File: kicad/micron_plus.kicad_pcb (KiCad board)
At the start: 2 copper layers, 163.8 x 123.2 mm, 87 parts, among them J1 Conn_02x17_Odd_Even, J2 Cliff DC10A, Q1 2N2905A, Q2 2N2905A, Q3 2N3904, Q4 2N3904, U1 MC68A21, U10 74LS00, U11 7406, U12 HM6264LP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

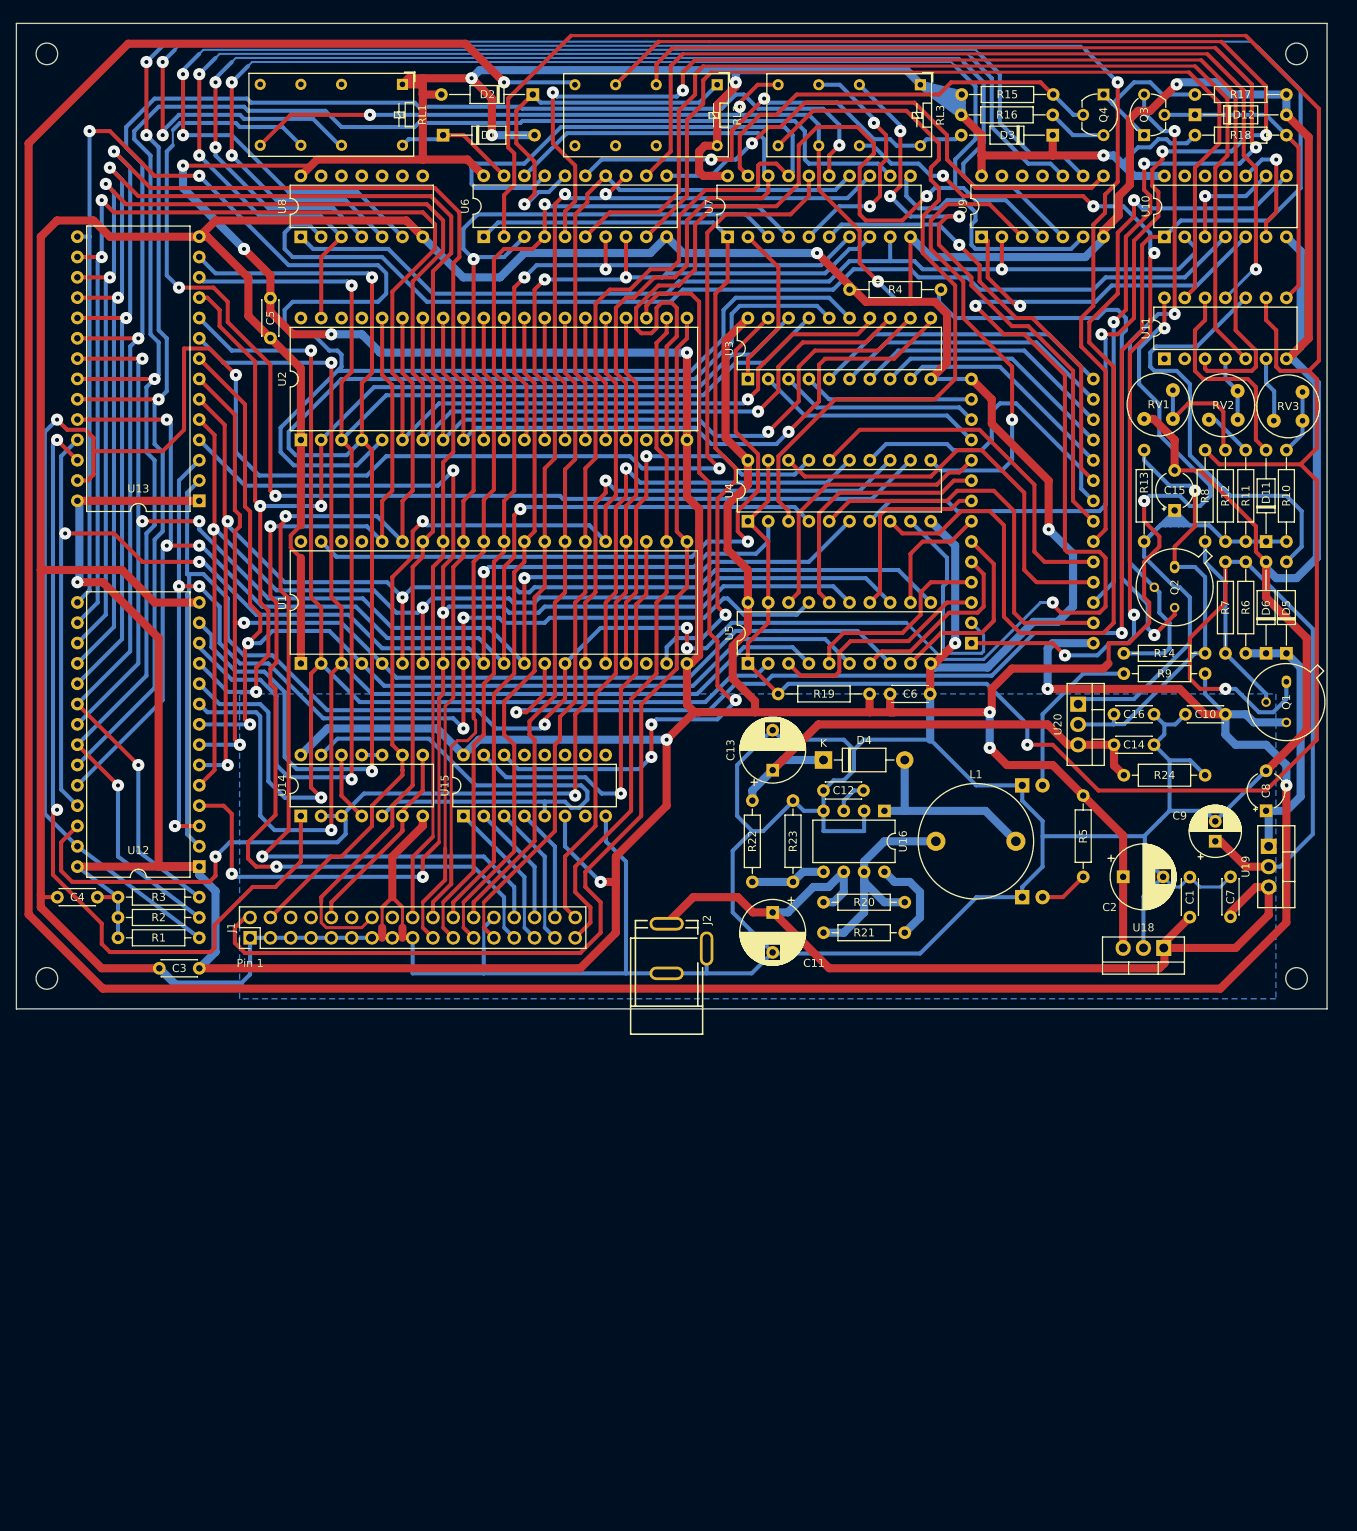
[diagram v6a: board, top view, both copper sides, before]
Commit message: KiCAD: Add heatsinks
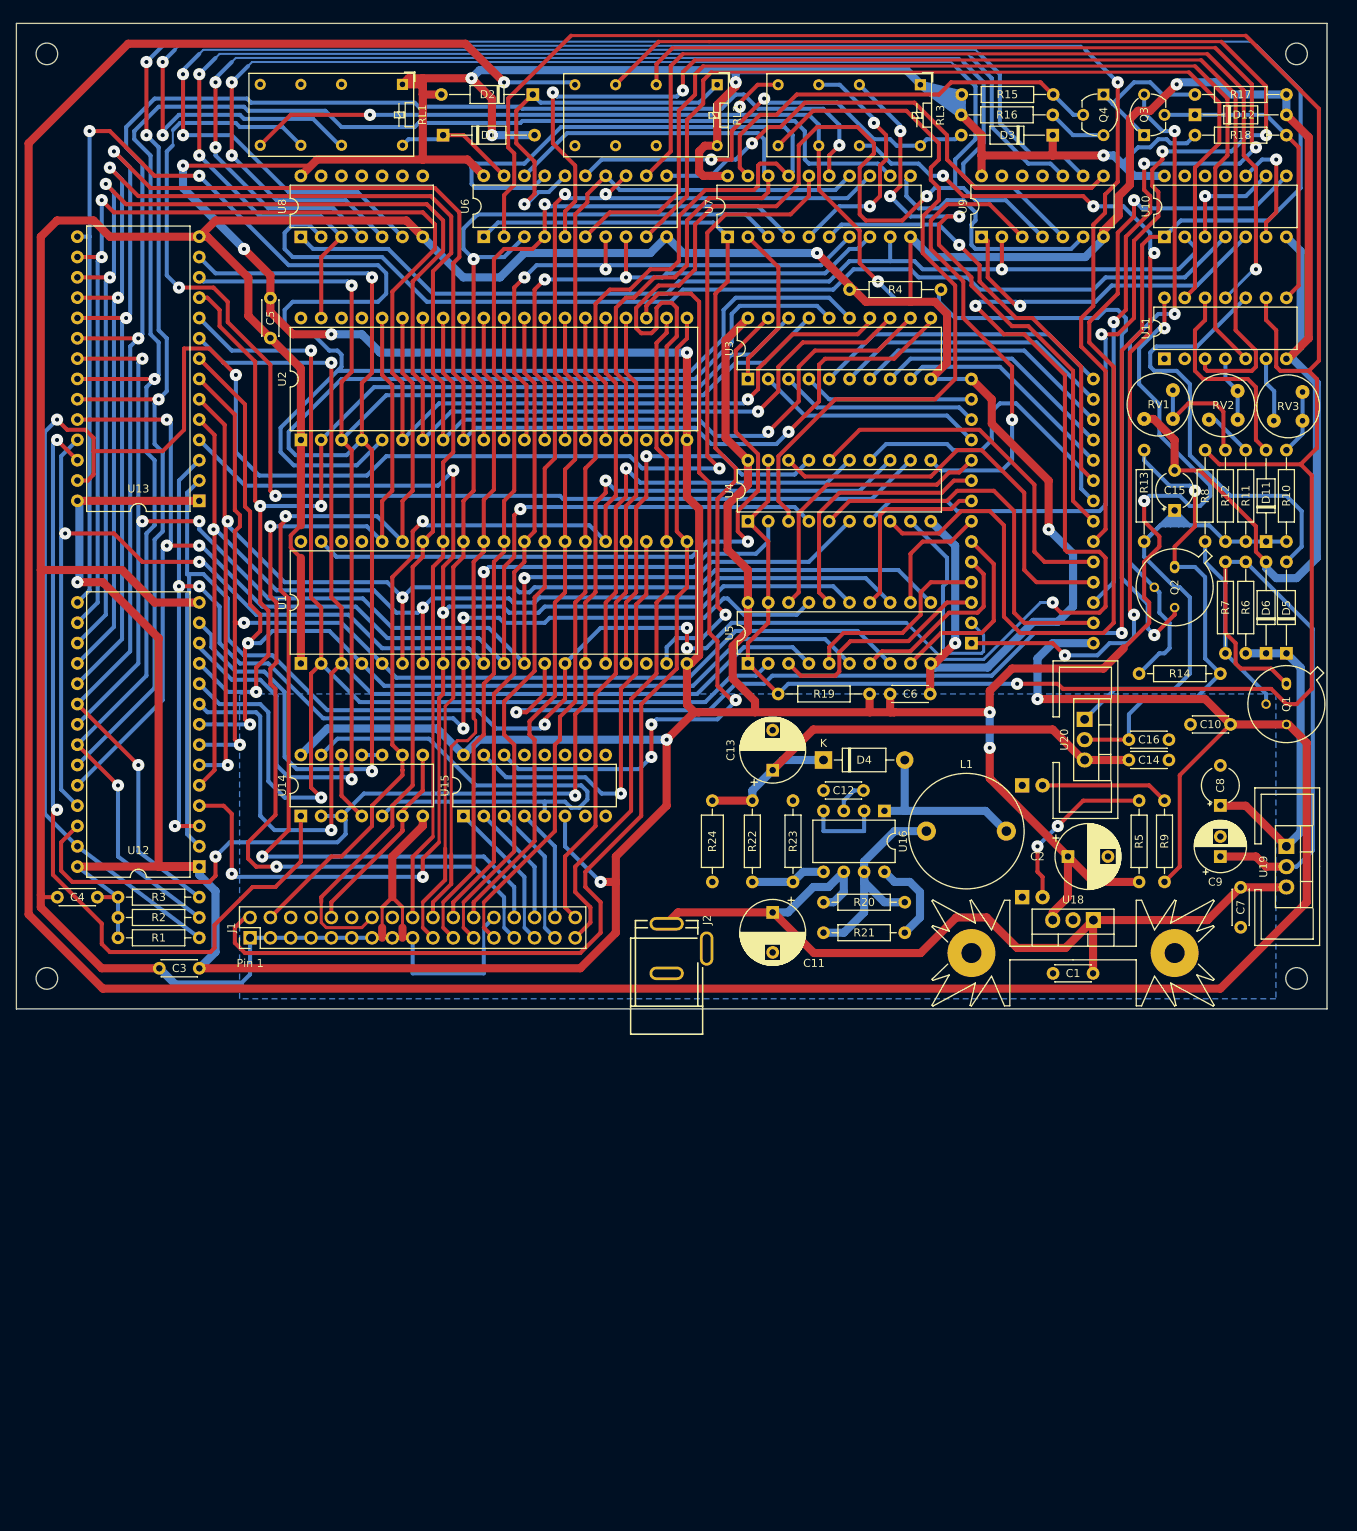
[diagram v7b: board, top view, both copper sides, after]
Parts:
- added HS1: Multicomp Pro MC33263, custom_footprints:Heatsink_Fischer_SK104-STC-STIC_35x13mm_2xDrill2.5mm, F.Cu at (172.7, 137.8)
- added HS2: Clip On Heatsink, custom_footprints:Heatsink_Boyd_PF720, F.Cu at (199.4, 124.5)
- added HS3: Clip On Heatsink, custom_footprints:Heatsink_Boyd_PF720, F.Cu at (174.2, 108.6)
- C12: value 470p -> 390p
- R22: value 12K -> 47K
- R23: value 560 -> 2K2
- moved R24 63.0 mm to (127.6, 128.9), turned to 90 degrees
- moved R9 26.5 mm to (184.2, 128.9), turned to 90 degrees
- moved C1 14.0 mm to (175.2, 140.3), turned to 180 degrees
- moved R5 12.9 mm to (181.0, 128.9), turned to 90 degrees
- moved U18 9.47 mm to (175.3, 133.7)
- moved C2 7.35 mm to (172.1, 125.7)
- moved C8 5.75 mm to (191.1, 119.3)
- moved C7 3.90 mm to (193.7, 129.6), turned to -90 degrees
- moved C16 3.68 mm to (179.7, 111.1)
- moved R14 3.18 mm to (191.1, 102.9)
- moved C14 2.67 mm to (179.7, 113.7)
- moved U19 2.21 mm to (199.4, 124.5)
- moved U20 2.07 mm to (174.2, 108.6)
- moved C9 2.01 mm to (191.1, 125.7)
- moved L1 1.74 mm to (154.4, 122.6)
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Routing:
- net GND: track 1000.8 -> 681.6 mm
- net Net-(D10-Pad2): track 6.13 -> 21.7 mm, vias 0 -> 2
- net /Main Logic and Eprom Socket/EpromVCC: track 416.2 -> 431.4 mm, vias 3 -> 2
- net /Control Latches/nVCCEnable: track 345.5 -> 330.5 mm
- net Net-(C9-Pad1): track 88.3 -> 75.6 mm, vias 1 -> 0
- net Net-(C8-Pad1): track 33.4 -> 41.0 mm
- net /Power Supply/9VDC: track 115.5 -> 109.8 mm
- net Net-(D7-Pad2): track 21.2 -> 16.0 mm
- net Net-(C16-Pad1): track 54.4 -> 59.2 mm
- net Net-(C15-Pad1): track 65.9 -> 69.0 mm
- net /Power Supply/28VDC: track 62.1 -> 65.0 mm
- net Net-(D4-Pad2): track 24.4 -> 22.6 mm
- net Net-(Q2-Pad2): track 83.2 -> 82.4 mm
- net Net-(L1-Pad1): track 29.9 -> 29.2 mm

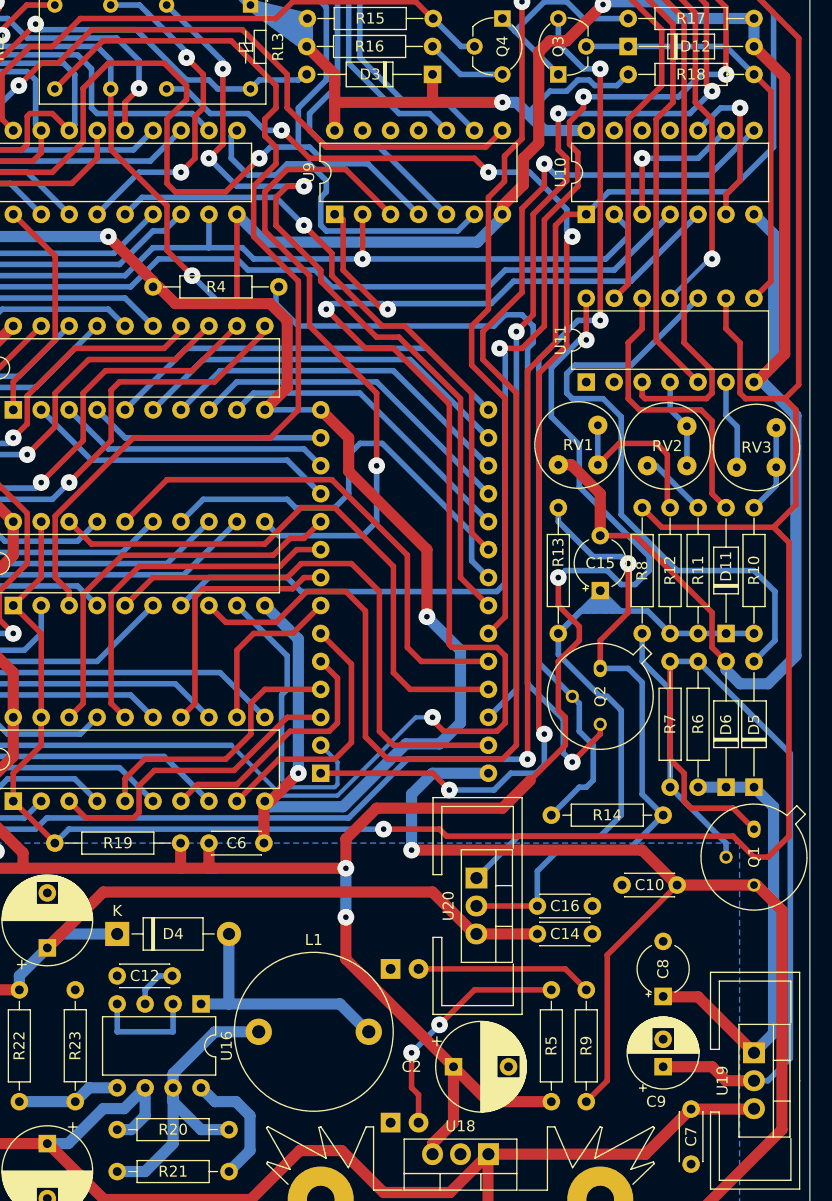
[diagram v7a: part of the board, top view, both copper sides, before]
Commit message: KiCAD: Trimmers now Bourns 3296W
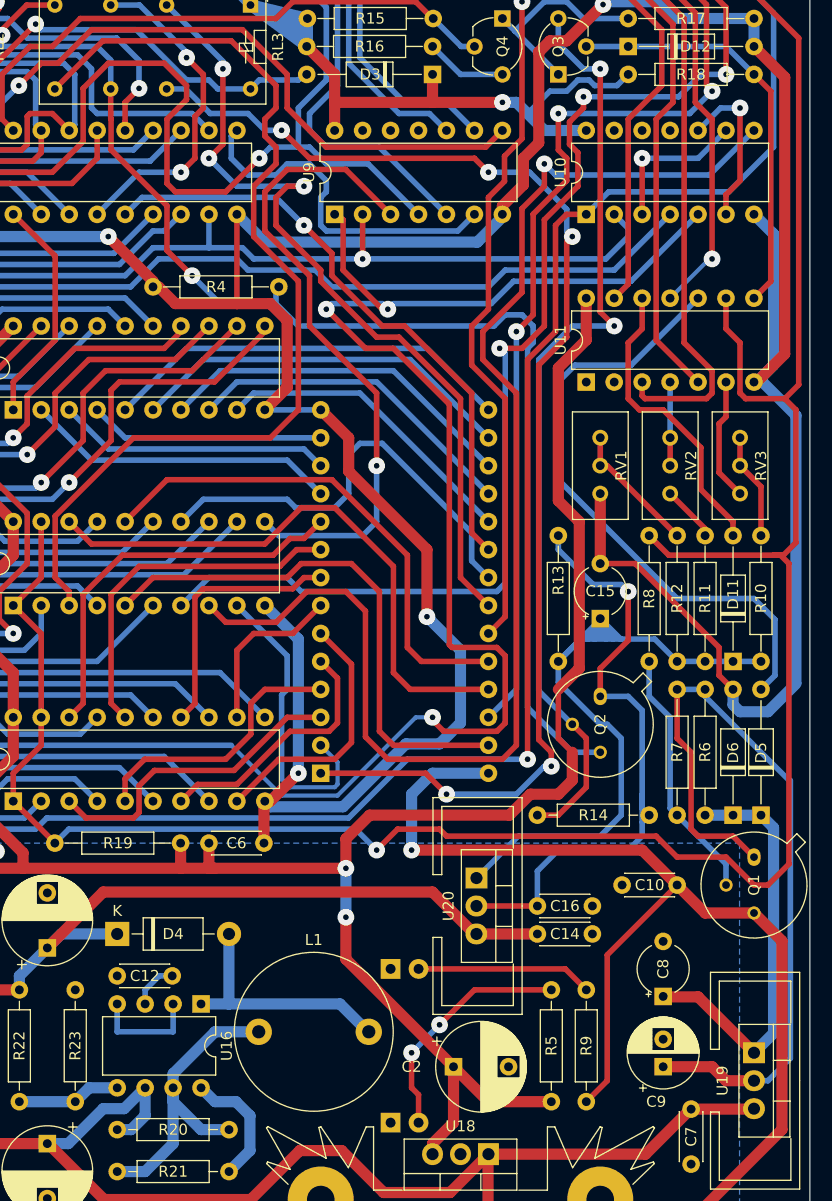
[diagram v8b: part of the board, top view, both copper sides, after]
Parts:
- RV1, RV2, RV3: footprint custom_footprints:Potentiometer_Bourns_3339P_Vertical_HandSoldering -> Potentiometer_THT:Potentiometer_Bourns_3296W_Vertical
- moved RV3 3.41 mm to (198.1, 68.6), turned to 90 degrees
- moved D11 2.62 mm to (197.5, 88.9)
- moved D5 2.62 mm to (200.0, 102.9)
- moved D6 2.62 mm to (197.5, 102.9)
- moved R8 2.62 mm to (189.9, 88.9)
- moved R10 2.62 mm to (200.0, 77.5)
- moved R11 2.62 mm to (194.9, 77.5)
- moved R12 2.62 mm to (192.4, 77.5)
- moved R6 2.62 mm to (194.9, 91.4)
- moved R7 2.62 mm to (192.4, 91.4)
- moved C15 2.54 mm to (185.4, 85.0)
- moved Q1 2.54 mm to (199.4, 106.7)
- moved Q2 2.54 mm to (185.4, 92.1)
- moved R13 2.54 mm to (181.6, 77.5)
- moved RV2 1.85 mm to (191.8, 68.6), turned to 90 degrees
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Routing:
- net VCC: track 836.2 -> 825.7 mm, vias 15 -> 13
- net /Control Latches/nVCCEnable: track 330.5 -> 335.9 mm
- net Net-(R12-Pad1): track 15.7 -> 12.2 mm
- net Net-(C9-Pad1): track 75.6 -> 72.3 mm
- net Net-(RV3-Pad3): track 8.11 -> 11.2 mm
- net Net-(Q2-Pad2): track 82.4 -> 85.2 mm
- net /Main Logic and Eprom Socket/EpromVPP: track 182.8 -> 180.0 mm, vias 4 -> 3
- net Net-(C8-Pad1): track 41.0 -> 38.2 mm
- net Net-(C15-Pad1): track 69.0 -> 67.1 mm
- net /Main Logic and Eprom Socket/EpromVCC: track 431.4 -> 429.8 mm
- net Net-(R10-Pad1): track 8.10 -> 9.69 mm
- net /Main Logic and Eprom Socket/Eprom1VPP: track 114.9 -> 116.2 mm
- net Net-(D5-Pad2): track 55.3 -> 56.3 mm
- net Net-(R11-Pad1): track 6.19 -> 5.13 mm
- net Net-(C16-Pad1): track 59.2 -> 58.2 mm
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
